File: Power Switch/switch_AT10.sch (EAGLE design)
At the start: 16 parts, among them U2 ATTINY10-TS8R

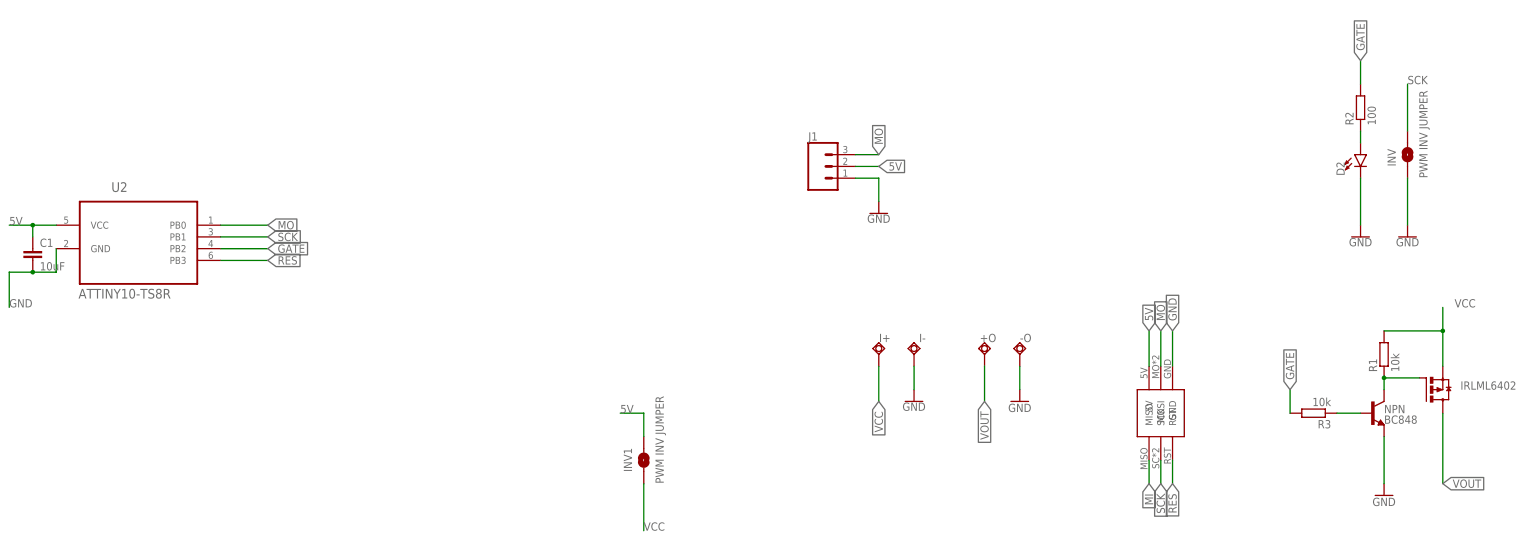
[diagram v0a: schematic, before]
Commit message: PCB updates (jumper distance) and a new RGB mini board
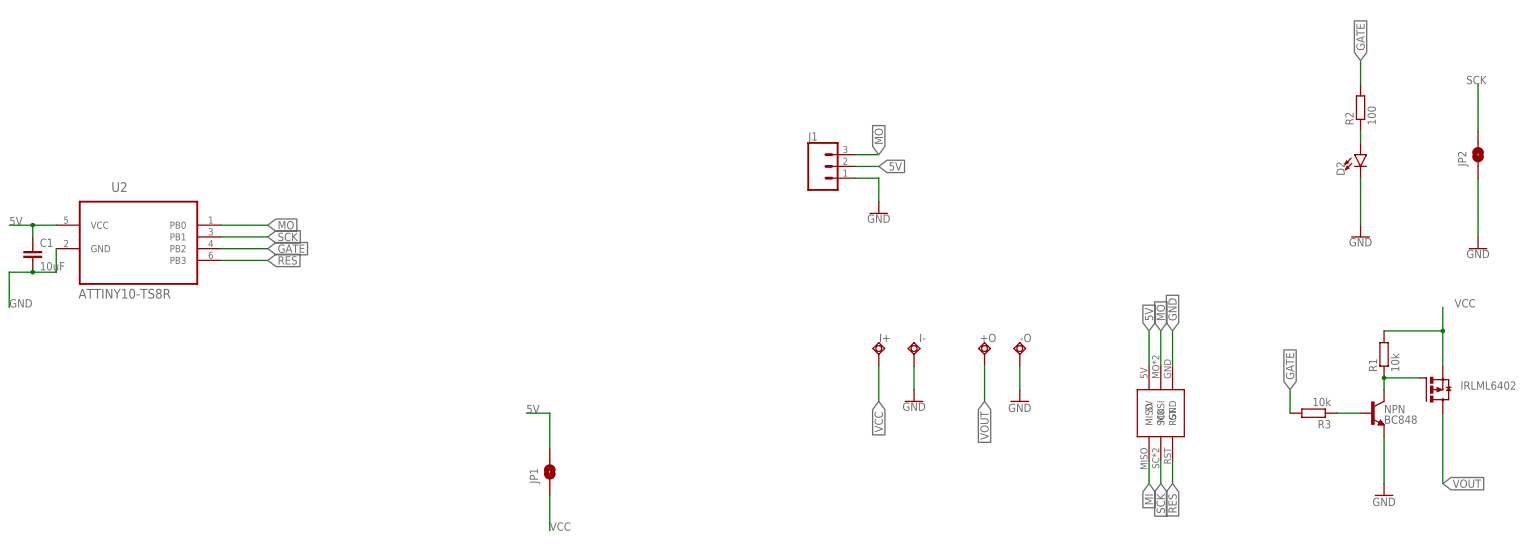
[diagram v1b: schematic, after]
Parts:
- removed INV, INV1: PWM INV JUMPER, SparkFun-Jumpers:JUMPER-SMT_2_NO_NO-SILK
- added JP1, JP2: JUMPER-SMT_2_NO_NO-SILK, SparkFun-Jumpers:JUMPER-SMT_2_NO_NO-SILK
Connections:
- net 5V: now also JP1.2; no longer INV1.2
- net GND: now also JP2.1; no longer INV.1
- net SCK: now also JP2.2; no longer INV.2
- net VCC: now also JP1.1; no longer INV1.1
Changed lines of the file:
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@@
 <part name="R3" library="rcl" library_urn="urn:adsk.eagle:library:334" deviceset="R-EU_" device="R0603" package3d_urn="urn:adsk.eagle:package:23555/2" value="10k"/>
 <part name="NPN" library="SparkFun-DiscreteSemi" library_urn="urn:adsk.eagle:library:514" deviceset="TRANS_NPN" device="-MMBT2222AL" package3d_urn="urn:adsk.eagle:package:38446/1" value="BC848"/>
-<part name="GND9" library="SparkFun-PowerSymbols" library_urn="urn:adsk.eagle:library:530" deviceset="GND" device=""/>
-<part name="INV" library="SparkFun-Jumpers" library_urn="urn:adsk.eagle:library:528" deviceset="JUMPER-SMT_2_NO" device="_NO-SILK" package3d_urn="urn:adsk.eagle:package:39277/1" value="PWM INV JUMPER"/>
-<part name="INV1" library="SparkFun-Jumpers" library_urn="urn:adsk.eagle:library:528" deviceset="JUMPER-SMT_2_NO" device="_NO-SILK" package3d_urn="urn:adsk.eagle:package:39277/1" value="PWM INV JUMPER"/>
 <part name="U$2" library="CoreDuino" deviceset="ISCP_PORT" device="POGONEW"/>
 <part name="U2" library="ATTINY10-TS8R" deviceset="ATTINY10-TS8R" device=""/>
+<part name="JP1" library="SparkFun-Jumpers" deviceset="JUMPER-SMT_2_NO" device="_NO-SILK" package3d_urn="urn:adsk.eagle:package:39277/1"/>
+<part name="JP2" library="SparkFun-Jumpers" deviceset="JUMPER-SMT_2_NO" device="_NO-SILK" package3d_urn="urn:adsk.eagle:package:39277/1"/>
+<part name="GND2" library="SparkFun-PowerSymbols" library_urn="urn:adsk.eagle:library:530" deviceset="GND" device=""/>
 </parts>
 <sheets>
@@
 <attribute name="VALUE" x="111.76" y="20.574" size="1.778" layer="96" font="vector"/>
 </instance>
-<instance part="GND9" gate="1" x="116.84" y="60.96" smashed="yes">
-<attribute name="VALUE" x="116.84" y="60.706" size="1.778" layer="96" align="top-center"/>
-</instance>
-<instance part="INV" gate="G$1" x="116.84" y="78.74" smashed="yes" rot="R90">
-<attribute name="NAME" x="114.3" y="76.2" size="1.778" layer="95" font="vector" rot="R90"/>
-<attribute name="VALUE" x="119.38" y="73.66" size="1.778" layer="96" font="vector" rot="R90" align="top-left"/>
-</instance>
-<instance part="INV1" gate="G$1" x="-48.26" y="12.7" smashed="yes" rot="R90">
-<attribute name="NAME" x="-50.8" y="10.16" size="1.778" layer="95" font="vector" rot="R90"/>
-<attribute name="VALUE" x="-45.72" y="7.62" size="1.778" layer="96" font="vector" rot="R90" align="top-left"/>
-</instance>
 <instance part="U$2" gate="G$1" x="58.42" y="27.94" smashed="yes"/>
 <instance part="U2" gate="A" x="-157.48" y="63.5" smashed="yes">
 <attribute name="NAME" x="-163.36345" y="70.682390625" size="2.0885" layer="95" ratio="10" rot="SR0"/>
 <attribute name="VALUE" x="-170.46203125" y="47.6387" size="2.08421875" layer="96" ratio="10" rot="SR0"/>
+</instance>
+<instance part="JP1" gate="G$1" x="-68.58" y="10.16" smashed="yes" rot="R90">
+<attribute name="NAME" x="-71.12" y="7.62" size="1.778" layer="95" font="vector" rot="R90"/>
+</instance>
+<instance part="JP2" gate="G$1" x="132.08" y="78.74" smashed="yes" rot="R90">
+<attribute name="NAME" x="129.54" y="76.2" size="1.778" layer="95" font="vector" rot="R90"/>
+</instance>
+<instance part="GND2" gate="1" x="132.08" y="58.42" smashed="yes">
+<attribute name="VALUE" x="132.08" y="58.166" size="1.778" layer="96" align="top-center"/>
 </instance>
 </instances>
@@
 <wire x1="-2.54" y1="76.2" x2="2.54" y2="76.2" width="0.1524" layer="91"/>
 <label x="2.54" y="76.2" size="1.778" layer="95" xref="yes"/>
-</segment>
-<segment>
-<pinref part="INV1" gate="G$1" pin="2"/>
-<wire x1="-48.26" y1="17.78" x2="-48.26" y2="22.86" width="0.1524" layer="91"/>
-<wire x1="-48.26" y1="22.86" x2="-53.34" y2="22.86" width="0.1524" layer="91"/>
-<label x="-53.34" y="22.86" size="1.778" layer="95"/>
 </segment>
 <segment>
@@
 <junction x="-180.34" y="63.5"/>
 </segment>
+<segment>
+<wire x1="-73.66" y1="22.86" x2="-68.58" y2="22.86" width="0.1524" layer="91"/>
+<pinref part="JP1" gate="G$1" pin="2"/>
+<wire x1="-68.58" y1="22.86" x2="-68.58" y2="15.24" width="0.1524" layer="91"/>
+<label x="-73.66" y="22.86" size="1.778" layer="95"/>
+</segment>
 </net>
 <net name="GND" class="0">
@@
 <pinref part="NPN" gate="G$1" pin="E"/>
 <wire x1="111.76" y1="17.78" x2="111.76" y2="7.62" width="0.1524" layer="91"/>
-</segment>
-<segment>
-<pinref part="GND9" gate="1" pin="GND"/>
-<wire x1="116.84" y1="63.5" x2="116.84" y2="73.66" width="0.1524" layer="91"/>
-<pinref part="INV" gate="G$1" pin="1"/>
 </segment>
 <segment>
@@
 <junction x="-180.34" y="53.34"/>
 </segment>
+<segment>
+<pinref part="JP2" gate="G$1" pin="1"/>
+<wire x1="132.08" y1="73.66" x2="132.08" y2="60.96" width="0.1524" layer="91"/>
+<pinref part="GND2" gate="1" pin="GND"/>
+</segment>
 </net>
 <net name="N$4" class="0">
@@
 <wire x1="2.54" y1="33.02" x2="2.54" y2="25.4" width="0.1524" layer="91"/>
 <label x="2.54" y="25.4" size="1.778" layer="95" rot="R270" xref="yes"/>
-</segment>
-<segment>
-<pinref part="INV1" gate="G$1" pin="1"/>
-<wire x1="-48.26" y1="7.62" x2="-48.26" y2="-2.54" width="0.1524" layer="91"/>
-<label x="-48.26" y="-2.54" size="1.778" layer="95"/>
 </segment>
 <segment>
@@
 <label x="127" y="45.72" size="1.778" layer="95"/>
 </segment>
+<segment>
+<pinref part="JP1" gate="G$1" pin="1"/>
+<wire x1="-68.58" y1="5.08" x2="-68.58" y2="-2.54" width="0.1524" layer="91"/>
+<label x="-68.58" y="-2.54" size="1.778" layer="95"/>
+</segment>
 </net>
 <net name="GATE" class="0">
@@
 </segment>
 <segment>
-<pinref part="INV" gate="G$1" pin="2"/>
-<wire x1="116.84" y1="83.82" x2="116.84" y2="93.98" width="0.1524" layer="91"/>
-<label x="116.84" y="93.98" size="1.778" layer="95"/>
-</segment>
-<segment>
 <wire x1="63.5" y1="12.7" x2="63.5" y2="7.62" width="0.1524" layer="91"/>
 <label x="63.5" y="7.62" size="1.778" layer="95" rot="R270" xref="yes"/>
 <pinref part="U$2" gate="G$1" pin="SCK"/>
 </segment>
-</net>
+<segment>
+<pinref part="JP2" gate="G$1" pin="2"/>
+<wire x1="132.08" y1="83.82" x2="132.08" y2="93.98" width="0.1524" layer="91"/>
+<label x="129.54" y="93.98" size="1.778" layer="95"/>
+</segment>
+</net>

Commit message: update
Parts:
- removed JP1, JP2: JUMPER-SMT_2_NO_NO-SILK, SparkFun-Jumpers:JUMPER-SMT_2_NO_NO-SILK
- added INV, INV1: PWM INV JUMPER, SparkFun-Jumpers:JUMPER-SMT_2_NO_NO-SILK
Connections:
- net 5V: now also INV1.2; no longer JP1.2
- net GND: now also INV.1; no longer JP2.1
- net SCK: now also INV.2; no longer JP2.2
- net VCC: now also INV1.1; no longer JP1.1
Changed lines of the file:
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@@
 <part name="R3" library="rcl" library_urn="urn:adsk.eagle:library:334" deviceset="R-EU_" device="R0603" package3d_urn="urn:adsk.eagle:package:23555/2" value="10k"/>
 <part name="NPN" library="SparkFun-DiscreteSemi" library_urn="urn:adsk.eagle:library:514" deviceset="TRANS_NPN" device="-MMBT2222AL" package3d_urn="urn:adsk.eagle:package:38446/1" value="BC848"/>
+<part name="GND9" library="SparkFun-PowerSymbols" library_urn="urn:adsk.eagle:library:530" deviceset="GND" device=""/>
+<part name="INV" library="SparkFun-Jumpers" library_urn="urn:adsk.eagle:library:528" deviceset="JUMPER-SMT_2_NO" device="_NO-SILK" package3d_urn="urn:adsk.eagle:package:39277/1" value="PWM INV JUMPER"/>
+<part name="INV1" library="SparkFun-Jumpers" library_urn="urn:adsk.eagle:library:528" deviceset="JUMPER-SMT_2_NO" device="_NO-SILK" package3d_urn="urn:adsk.eagle:package:39277/1" value="PWM INV JUMPER"/>
 <part name="U$2" library="CoreDuino" deviceset="ISCP_PORT" device="POGONEW"/>
 <part name="U2" library="ATTINY10-TS8R" deviceset="ATTINY10-TS8R" device=""/>
-<part name="JP1" library="SparkFun-Jumpers" deviceset="JUMPER-SMT_2_NO" device="_NO-SILK" package3d_urn="urn:adsk.eagle:package:39277/1"/>
-<part name="JP2" library="SparkFun-Jumpers" deviceset="JUMPER-SMT_2_NO" device="_NO-SILK" package3d_urn="urn:adsk.eagle:package:39277/1"/>
-<part name="GND2" library="SparkFun-PowerSymbols" library_urn="urn:adsk.eagle:library:530" deviceset="GND" device=""/>
 </parts>
 <sheets>
@@
 <attribute name="VALUE" x="111.76" y="20.574" size="1.778" layer="96" font="vector"/>
 </instance>
+<instance part="GND9" gate="1" x="116.84" y="60.96" smashed="yes">
+<attribute name="VALUE" x="116.84" y="60.706" size="1.778" layer="96" align="top-center"/>
+</instance>
+<instance part="INV" gate="G$1" x="116.84" y="78.74" smashed="yes" rot="R90">
+<attribute name="NAME" x="114.3" y="76.2" size="1.778" layer="95" font="vector" rot="R90"/>
+<attribute name="VALUE" x="119.38" y="73.66" size="1.778" layer="96" font="vector" rot="R90" align="top-left"/>
+</instance>
+<instance part="INV1" gate="G$1" x="-48.26" y="12.7" smashed="yes" rot="R90">
+<attribute name="NAME" x="-50.8" y="10.16" size="1.778" layer="95" font="vector" rot="R90"/>
+<attribute name="VALUE" x="-45.72" y="7.62" size="1.778" layer="96" font="vector" rot="R90" align="top-left"/>
+</instance>
 <instance part="U$2" gate="G$1" x="58.42" y="27.94" smashed="yes"/>
 <instance part="U2" gate="A" x="-157.48" y="63.5" smashed="yes">
 <attribute name="NAME" x="-163.36345" y="70.682390625" size="2.0885" layer="95" ratio="10" rot="SR0"/>
 <attribute name="VALUE" x="-170.46203125" y="47.6387" size="2.08421875" layer="96" ratio="10" rot="SR0"/>
-</instance>
-<instance part="JP1" gate="G$1" x="-68.58" y="10.16" smashed="yes" rot="R90">
-<attribute name="NAME" x="-71.12" y="7.62" size="1.778" layer="95" font="vector" rot="R90"/>
-</instance>
-<instance part="JP2" gate="G$1" x="132.08" y="78.74" smashed="yes" rot="R90">
-<attribute name="NAME" x="129.54" y="76.2" size="1.778" layer="95" font="vector" rot="R90"/>
-</instance>
-<instance part="GND2" gate="1" x="132.08" y="58.42" smashed="yes">
-<attribute name="VALUE" x="132.08" y="58.166" size="1.778" layer="96" align="top-center"/>
 </instance>
 </instances>
@@
 <wire x1="-2.54" y1="76.2" x2="2.54" y2="76.2" width="0.1524" layer="91"/>
 <label x="2.54" y="76.2" size="1.778" layer="95" xref="yes"/>
+</segment>
+<segment>
+<pinref part="INV1" gate="G$1" pin="2"/>
+<wire x1="-48.26" y1="17.78" x2="-48.26" y2="22.86" width="0.1524" layer="91"/>
+<wire x1="-48.26" y1="22.86" x2="-53.34" y2="22.86" width="0.1524" layer="91"/>
+<label x="-53.34" y="22.86" size="1.778" layer="95"/>
 </segment>
 <segment>
@@
 <junction x="-180.34" y="63.5"/>
 </segment>
-<segment>
-<wire x1="-73.66" y1="22.86" x2="-68.58" y2="22.86" width="0.1524" layer="91"/>
-<pinref part="JP1" gate="G$1" pin="2"/>
-<wire x1="-68.58" y1="22.86" x2="-68.58" y2="15.24" width="0.1524" layer="91"/>
-<label x="-73.66" y="22.86" size="1.778" layer="95"/>
-</segment>
 </net>
 <net name="GND" class="0">
@@
 <pinref part="NPN" gate="G$1" pin="E"/>
 <wire x1="111.76" y1="17.78" x2="111.76" y2="7.62" width="0.1524" layer="91"/>
+</segment>
+<segment>
+<pinref part="GND9" gate="1" pin="GND"/>
+<wire x1="116.84" y1="63.5" x2="116.84" y2="73.66" width="0.1524" layer="91"/>
+<pinref part="INV" gate="G$1" pin="1"/>
 </segment>
 <segment>
@@
 <junction x="-180.34" y="53.34"/>
 </segment>
-<segment>
-<pinref part="JP2" gate="G$1" pin="1"/>
-<wire x1="132.08" y1="73.66" x2="132.08" y2="60.96" width="0.1524" layer="91"/>
-<pinref part="GND2" gate="1" pin="GND"/>
-</segment>
 </net>
 <net name="N$4" class="0">
@@
 <wire x1="2.54" y1="33.02" x2="2.54" y2="25.4" width="0.1524" layer="91"/>
 <label x="2.54" y="25.4" size="1.778" layer="95" rot="R270" xref="yes"/>
+</segment>
+<segment>
+<pinref part="INV1" gate="G$1" pin="1"/>
+<wire x1="-48.26" y1="7.62" x2="-48.26" y2="-2.54" width="0.1524" layer="91"/>
+<label x="-48.26" y="-2.54" size="1.778" layer="95"/>
 </segment>
 <segment>
@@
 <label x="127" y="45.72" size="1.778" layer="95"/>
 </segment>
-<segment>
-<pinref part="JP1" gate="G$1" pin="1"/>
-<wire x1="-68.58" y1="5.08" x2="-68.58" y2="-2.54" width="0.1524" layer="91"/>
-<label x="-68.58" y="-2.54" size="1.778" layer="95"/>
-</segment>
 </net>
 <net name="GATE" class="0">
@@
 <segment>
 <pinref part="U2" gate="A" pin="PB2"/>
-<wire x1="-139.7" y1="58.42" x2="-129.54" y2="58.42" width="0.1524" layer="91"/>
-<label x="-129.54" y="58.42" size="1.778" layer="95" xref="yes"/>
+<wire x1="-139.7" y1="58.42" x2="-121.92" y2="58.42" width="0.1524" layer="91"/>
+<label x="-121.92" y="58.42" size="1.778" layer="95" xref="yes"/>
 </segment>
 </net>
@@
 <segment>
 <pinref part="U2" gate="A" pin="PB0"/>
-<wire x1="-139.7" y1="63.5" x2="-129.54" y2="63.5" width="0.1524" layer="91"/>
-<label x="-129.54" y="63.5" size="1.778" layer="95" xref="yes"/>
+<wire x1="-139.7" y1="63.5" x2="-121.92" y2="63.5" width="0.1524" layer="91"/>
+<label x="-121.92" y="63.5" size="1.778" layer="95" xref="yes"/>
 </segment>
 <segment>
@@
 <segment>
 <pinref part="U2" gate="A" pin="PB1"/>
-<wire x1="-139.7" y1="60.96" x2="-129.54" y2="60.96" width="0.1524" layer="91"/>
-<label x="-129.54" y="60.96" size="1.778" layer="95" xref="yes"/>
+<wire x1="-139.7" y1="60.96" x2="-121.92" y2="60.96" width="0.1524" layer="91"/>
+<label x="-121.92" y="60.96" size="1.778" layer="95" xref="yes"/>
+</segment>
+<segment>
+<pinref part="INV" gate="G$1" pin="2"/>
+<wire x1="116.84" y1="83.82" x2="116.84" y2="93.98" width="0.1524" layer="91"/>
+<label x="116.84" y="93.98" size="1.778" layer="95"/>
 </segment>
 <segment>
@@
 <pinref part="U$2" gate="G$1" pin="SCK"/>
 </segment>
-<segment>
-<pinref part="JP2" gate="G$1" pin="2"/>
-<wire x1="132.08" y1="83.82" x2="132.08" y2="93.98" width="0.1524" layer="91"/>
-<label x="129.54" y="93.98" size="1.778" layer="95"/>
-</segment>
-</net>
+</net>
